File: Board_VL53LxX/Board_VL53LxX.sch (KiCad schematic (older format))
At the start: 11 parts, among them J1 Conn_01x06, U1 VL53L0X

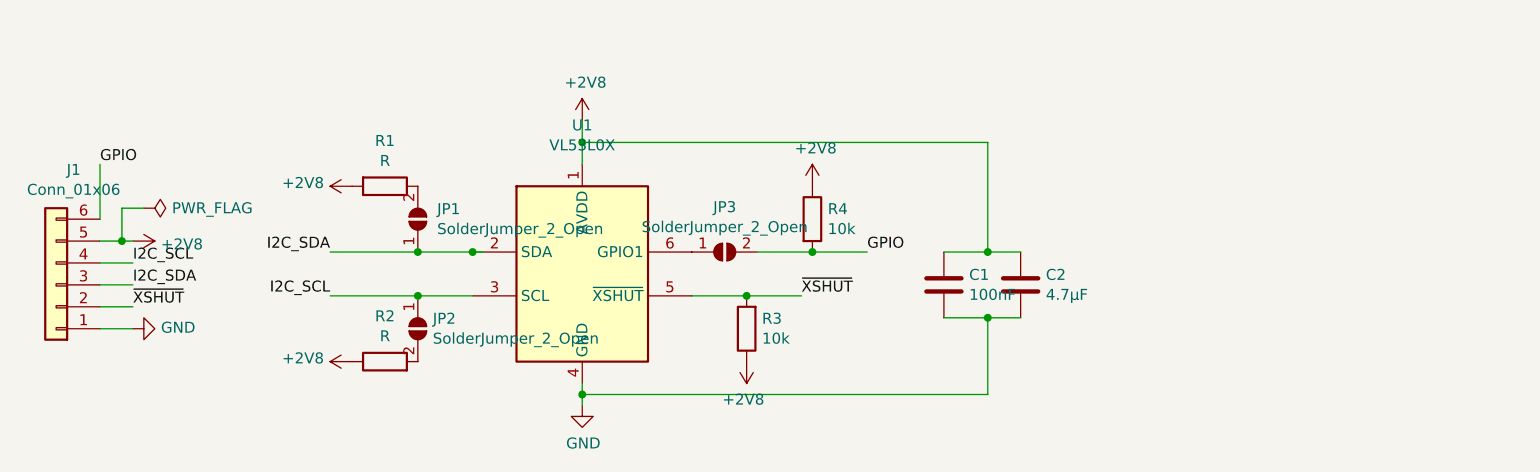
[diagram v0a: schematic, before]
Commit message: VL53L board routed
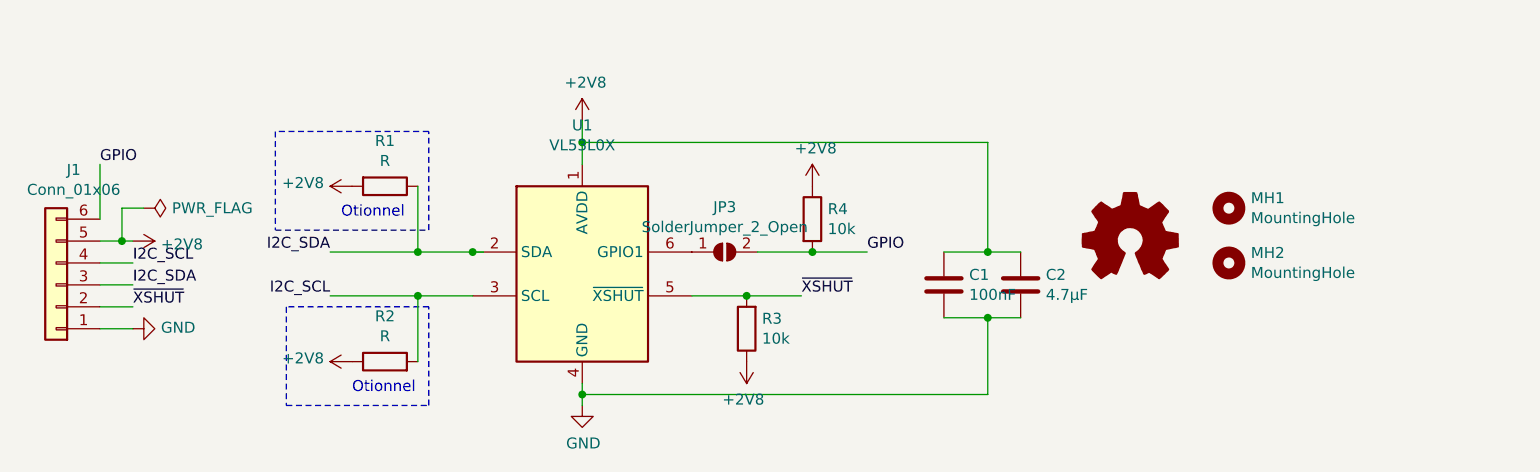
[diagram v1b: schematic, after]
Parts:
- removed JP1, JP2: SolderJumper_2_Open, Jumper:SolderJumper-2_P1.3mm_Open_TrianglePad1.0x1.5mm, symbol Jumper:SolderJumper_2_Open
- added MH1, MH2: MountingHole, MountingHole:MountingHole_2.2mm_M2, symbol Mechanical:MountingHole
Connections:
- wire segments 30 -> 32
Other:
- note added: "Otionnel"
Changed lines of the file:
@@
 	4300 3850 4250 3850
 Connection ~ 4250 3850
-Wire Wire Line
-	4250 3850 4000 3850
 $Comp
 L power:+2V8 #PWR05
@@
 I2C_SDA
 Wire Wire Line
-	3600 3850 4000 3850
-Connection ~ 4000 3850
-Wire Wire Line
 	6050 3850 5800 3850
 Connection ~ 5800 3850
-Connection ~ 4000 4050
-Wire Wire Line
-	4000 4050 4250 4050
-Wire Wire Line
-	3600 4050 4000 4050
 Connection ~ 5500 4050
 Wire Wire Line
@@
 	6600 4150 6750 4150
 Connection ~ 6600 4150
-$Comp
-L Jumper:SolderJumper_2_Open JP1
-U 1 1 5BC3B565
-P 4000 3700
-F 0 "JP1" V 4046 3612 50  0000 R CNN
-F 1 "SolderJumper_2_Open" V 3955 3612 50  0000 R CNN
-F 2 "Jumper:SolderJumper-2_P1.3mm_Open_TrianglePad1.0x1.5mm" H 4000 3700 50  0001 C CNN
-F 3 "~" H 4000 3700 50  0001 C CNN
-	1    4000 3700
-	0    -1   -1   0
-$EndComp
-$Comp
-L Jumper:SolderJumper_2_Open JP2
-U 1 1 5BC3B818
-P 4000 4200
-F 0 "JP2" V 3954 4268 50  0000 L CNN
-F 1 "SolderJumper_2_Open" V 4045 4268 50  0000 L CNN
-F 2 "Jumper:SolderJumper-2_P1.3mm_Open_TrianglePad1.0x1.5mm" H 4000 4200 50  0001 C CNN
-F 3 "~" H 4000 4200 50  0001 C CNN
-	1    4000 4200
-	0    1    1    0
-$EndComp
 $Comp
 L Connector_Generic:Conn_01x06 J1
@@
 Wire Wire Line
 	2550 4200 2700 4200
+Wire Wire Line
+	3600 3850 4000 3850
+Wire Wire Line
+	4000 3550 4000 3850
+Connection ~ 4000 3850
+Wire Wire Line
+	4000 3850 4250 3850
+Text Notes 3650 3700 0    50   ~ 0
+Otionnel
+Text Notes 3700 4500 0    50   ~ 0
+Otionnel
+Wire Wire Line
+	3600 4050 4000 4050
+Wire Wire Line
+	4000 4050 4000 4350
+Connection ~ 4000 4050
+Wire Wire Line
+	4000 4050 4250 4050
+Wire Notes Line
+	3350 3750 4050 3750
+Wire Notes Line
+	4050 3750 4050 3300
+Wire Notes Line
+	4050 3300 3350 3300
+Wire Notes Line
+	3350 3300 3350 3750
+Wire Notes Line
+	3400 4550 4050 4550
+Wire Notes Line
+	4050 4550 4050 4100
+Wire Notes Line
+	4050 4100 3400 4100
+Wire Notes Line
+	3400 4100 3400 4550
+$Comp
+L Mechanical:MountingHole MH1
+U 1 1 5BC3ACFC
+P 7700 3650
+F 0 "MH1" H 7800 3696 50  0000 L CNN
+F 1 "MountingHole" H 7800 3605 50  0000 L CNN
+F 2 "MountingHole:MountingHole_2.2mm_M2" H 7700 3650 50  0001 C CNN
+F 3 "~" H 7700 3650 50  0001 C CNN
+	1    7700 3650
+	1    0    0    -1
+$EndComp
+$Comp
+L Mechanical:MountingHole MH2
+U 1 1 5BC3AFD2
+P 7700 3900
+F 0 "MH2" H 7800 3946 50  0000 L CNN
+F 1 "MountingHole" H 7800 3855 50  0000 L CNN
+F 2 "MountingHole:MountingHole_2.2mm_M2" H 7700 3900 50  0001 C CNN
+F 3 "~" H 7700 3900 50  0001 C CNN
+	1    7700 3900
+	1    0    0    -1
+$EndComp
+$Comp
+L Graphic:Logo_Open_Hardware_Small #LOGO1
+U 1 1 5BC3B0F0
+P 7250 3800
+F 0 "#LOGO1" H 7250 4075 50  0001 C CNN
+F 1 "Logo_Open_Hardware_Small" H 7250 3575 50  0001 C CNN
+F 2 "" H 7250 3800 50  0001 C CNN
+F 3 "~" H 7250 3800 50  0001 C CNN
+	1    7250 3800
+	1    0    0    -1
+$EndComp
 $EndSCHEMATC

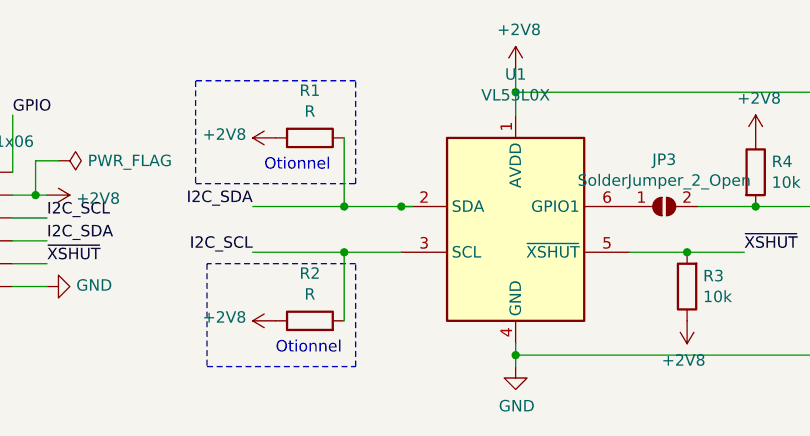
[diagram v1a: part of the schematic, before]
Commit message: Update VL53L0X PCB
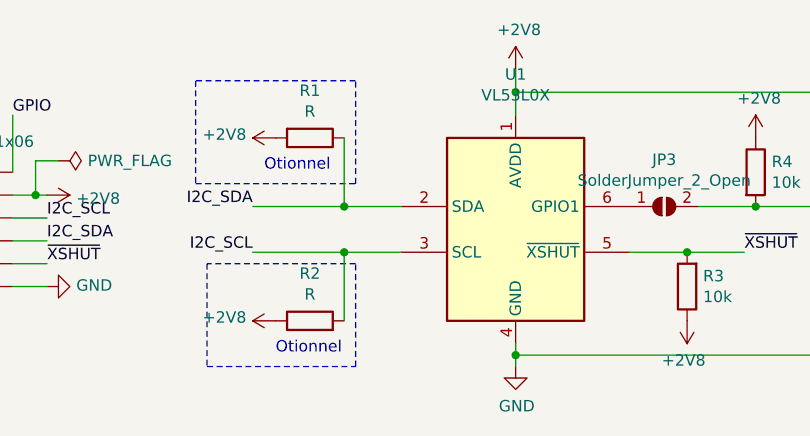
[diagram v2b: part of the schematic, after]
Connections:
- wire segments 32 -> 31
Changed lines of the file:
@@
 EESchema Schematic File Version 4
+LIBS:Board_VL53LxX-cache
 EELAYER 26 0
 EELAYER END
@@
 	-1   0    0    1
 $EndComp
-Wire Wire Line
-	4300 3850 4250 3850
-Connection ~ 4250 3850
 $Comp
 L power:+2V8 #PWR05

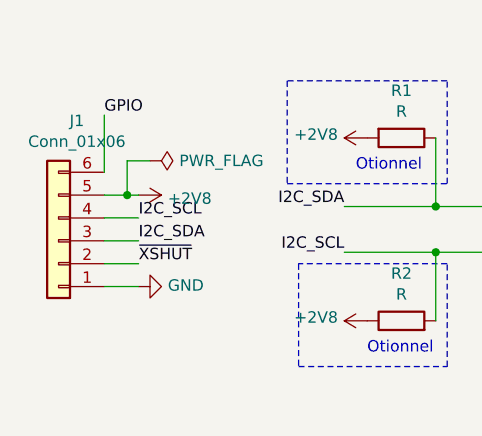
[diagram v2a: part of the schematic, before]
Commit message: Changed JST connectors
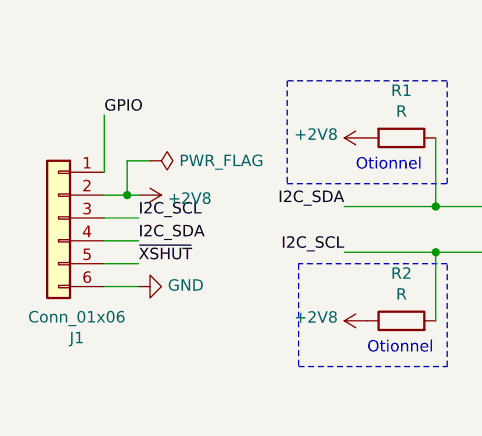
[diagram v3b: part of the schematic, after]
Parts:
- J1: footprint Connector_JST:JST_PH_B6B-PH-K_1x06_P2.00mm_Vertical -> Connector_JST:JST_PH_S6B-PH-K_1x06_P2.00mm_Horizontal
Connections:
- net +2V8: now also J1.2 (Pin_2); no longer J1.5 (Pin_5)
- net GND: now also J1.6 (Pin_6); no longer J1.1 (Pin_1)
- net GPIO: now also J1.1 (Pin_1); no longer J1.6 (Pin_6)
- net I2C_SCL: now also J1.3 (Pin_3); no longer J1.4 (Pin_4)
- net I2C_SDA: now also J1.4 (Pin_4); no longer J1.3 (Pin_3)
- net ~XSHUT: now also J1.5 (Pin_5); no longer J1.2 (Pin_2)
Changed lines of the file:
@@
 L Connector_Generic:Conn_01x06 J1
 U 1 1 5BC3B9FD
-P 2350 4000
-F 0 "J1" H 2270 3475 50  0000 C CNN
-F 1 "Conn_01x06" H 2270 3566 50  0000 C CNN
-F 2 "Connector_JST:JST_PH_B6B-PH-K_1x06_P2.00mm_Vertical" H 2350 4000 50  0001 C CNN
-F 3 "~" H 2350 4000 50  0001 C CNN
-	1    2350 4000
-	-1   0    0    1
+P 2350 3900
+F 0 "J1" H 2270 3375 50  0000 C CNN
+F 1 "Conn_01x06" H 2270 3466 50  0000 C CNN
+F 2 "Connector_JST:JST_PH_S6B-PH-K_1x06_P2.00mm_Horizontal" H 2350 3900 50  0001 C CNN
+F 3 "~" H 2350 3900 50  0001 C CNN
+	1    2350 3900
+	-1   0    0    -1
 $EndComp
 Text Label 2550 3450 0    50   ~ 0

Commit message: update board
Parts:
- removed MH1, MH2: MountingHole, MountingHole:MountingHole_2.2mm_M2, symbol Mechanical:MountingHole
- added LOGO1: Logo_Open_Hardware_Small, Symbol:OSHW-Logo2_7.3x6mm_SilkScreen, symbol Graphic:Logo_Open_Hardware_Small
- added LOGO2: Logo_Open_Hardware_Small, PhenixRobotik:Logo_8,5mm, symbol Graphic:Logo_Open_Hardware_Small
- added MH1, MH2: MountingHole_Pad, MountingHole:MountingHole_2.2mm_M2_Pad, symbol Mechanical:MountingHole_Pad
- U1: footprint PhoenixRobotik:TOF-12_4.4x2.4x1.0mm_P0.8mm -> PhenixRobotik:TOF-12_4.4x2.4x1.0mm_P0.8mm; symbol PhoenixRobotik:VL53L0X -> PhenixRobotik:VL53L0X
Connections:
- wire segments 31 -> 33
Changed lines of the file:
@@
 EESchema Schematic File Version 4
-LIBS:Board_VL53LxX-cache
 EELAYER 26 0
 EELAYER END
@@
 $EndDescr
 $Comp
-L PhoenixRobotik:VL53L0X U1
+L PhenixRobotik:VL53L0X U1
 U 1 1 5BC3718A
 P 4750 3950
 F 0 "U1" H 4750 4628 50  0000 C CNN
 F 1 "VL53L0X" H 4750 4537 50  0000 C CNN
-F 2 "PhoenixRobotik:TOF-12_4.4x2.4x1.0mm_P0.8mm" H 5950 3450 50  0001 C CNN
+F 2 "PhenixRobotik:TOF-12_4.4x2.4x1.0mm_P0.8mm" H 5950 3450 50  0001 C CNN
 F 3 "https://www.st.com/resource/en/datasheet/vl53l0x.pdf" H 5950 3350 50  0001 C CNN
 	1    4750 3950
@@
 	3400 4100 3400 4550
 $Comp
-L Mechanical:MountingHole MH1
-U 1 1 5BC3ACFC
-P 7700 3650
-F 0 "MH1" H 7800 3696 50  0000 L CNN
-F 1 "MountingHole" H 7800 3605 50  0000 L CNN
-F 2 "MountingHole:MountingHole_2.2mm_M2" H 7700 3650 50  0001 C CNN
-F 3 "~" H 7700 3650 50  0001 C CNN
-	1    7700 3650
-	1    0    0    -1
-$EndComp
-$Comp
-L Mechanical:MountingHole MH2
-U 1 1 5BC3AFD2
-P 7700 3900
-F 0 "MH2" H 7800 3946 50  0000 L CNN
-F 1 "MountingHole" H 7800 3855 50  0000 L CNN
-F 2 "MountingHole:MountingHole_2.2mm_M2" H 7700 3900 50  0001 C CNN
-F 3 "~" H 7700 3900 50  0001 C CNN
-	1    7700 3900
-	1    0    0    -1
-$EndComp
-$Comp
-L Graphic:Logo_Open_Hardware_Small #LOGO1
+L Graphic:Logo_Open_Hardware_Small LOGO1
 U 1 1 5BC3B0F0
-P 7250 3800
-F 0 "#LOGO1" H 7250 4075 50  0001 C CNN
-F 1 "Logo_Open_Hardware_Small" H 7250 3575 50  0001 C CNN
-F 2 "" H 7250 3800 50  0001 C CNN
-F 3 "~" H 7250 3800 50  0001 C CNN
-	1    7250 3800
-	1    0    0    -1
-$EndComp
+P 7200 3000
+F 0 "LOGO1" H 7200 3275 50  0001 C CNN
+F 1 "Logo_Open_Hardware_Small" H 7200 2775 50  0001 C CNN
+F 2 "Symbol:OSHW-Logo2_7.3x6mm_SilkScreen" H 7200 3000 50  0001 C CNN
+F 3 "~" H 7200 3000 50  0001 C CNN
+	1    7200 3000
+	1    0    0    -1
+$EndComp
+$Comp
+L Mechanical:MountingHole_Pad MH1
+U 1 1 5BE08298
+P 8450 3600
+F 0 "MH1" V 8404 3750 50  0000 L CNN
+F 1 "MountingHole_Pad" V 8495 3750 50  0000 L CNN
+F 2 "MountingHole:MountingHole_2.2mm_M2_Pad" H 8450 3600 50  0001 C CNN
+F 3 "~" H 8450 3600 50  0001 C CNN
+	1    8450 3600
+	0    1    1    0
+$EndComp
+$Comp
+L Mechanical:MountingHole_Pad MH2
+U 1 1 5BE08309
+P 8450 3800
+F 0 "MH2" V 8404 3950 50  0000 L CNN
+F 1 "MountingHole_Pad" V 8495 3950 50  0000 L CNN
+F 2 "MountingHole:MountingHole_2.2mm_M2_Pad" H 8450 3800 50  0001 C CNN
+F 3 "~" H 8450 3800 50  0001 C CNN
+	1    8450 3800
+	0    1    1    0
+$EndComp
+Wire Wire Line
+	8350 3600 8350 3800
+Connection ~ 8350 3800
+Wire Wire Line
+	8350 3800 8350 4000
+$Comp
+L power:GND #PWR0101
+U 1 1 5BE0885F
+P 8350 4000
+F 0 "#PWR0101" H 8350 3750 50  0001 C CNN
+F 1 "GND" H 8355 3827 50  0000 C CNN
+F 2 "" H 8350 4000 50  0001 C CNN
+F 3 "" H 8350 4000 50  0001 C CNN
+	1    8350 4000
+	1    0    0    -1
+$EndComp
+$Comp
+L Graphic:Logo_Open_Hardware_Small LOGO2
+U 1 1 5BE08D27
+P 7650 3000
+F 0 "LOGO2" H 7650 3275 50  0001 C CNN
+F 1 "Logo_Open_Hardware_Small" H 7650 2775 50  0001 C CNN
+F 2 "PhenixRobotik:Logo_8,5mm" H 7650 3000 50  0001 C CNN
+F 3 "~" H 7650 3000 50  0001 C CNN
+	1    7650 3000
+	1    0    0    -1
+$EndComp
